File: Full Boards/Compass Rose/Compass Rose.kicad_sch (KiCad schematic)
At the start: 249 parts, among them J1 Program Header, J3 Optional Bond, Q1 BSS314PE, Q2 DMN6075S, Q3 BSS314PE, Q4 DMN6075S, Q5 BSS314PE, Q6 DMN6075S, SW1 Boot, SW2 Reset, SW3 219-2MSTR

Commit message: Updated the 100uF caps to polymer.
Signed-off-by: digimer <digital.mermaid@gmail.com>
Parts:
- C19, C20, C21: footprint Capacitor_THT:CP_Radial_D8.0mm_P5.00mm -> Capacitor_THT:CP_Radial_D8.0mm_P3.50mm; Part Nichicon UPW1H101MPD1FA -> Kemet A7C0KS107M1HAAS031

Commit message: Swapped the 10uF cap to a ceramic.
Signed-off-by: digimer <digital.mermaid@gmail.com>
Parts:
- C5: footprint mr-stuff:Nichicon UBT -> mr-stuff:Kyocera AVX 1206; Part Nichicon UBT1H100MPD8 -> Kyocera 12105C106K4Z2A
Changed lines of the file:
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@@
 			)
 		)
-		(property "Footprint" "mr-stuff:Nichicon UBT"
+		(property "Footprint" "mr-stuff:Kyocera AVX 1206"
 			(at 200.3552 35.56 0)
 			(hide yes)
@@
 			)
 		)
-		(property "Datasheet" "https://www.nichicon.co.jp/english/series_items/catalog_pdf/e-ubt.pdf"
+		(property "Datasheet" "https://datasheets.kyocera-avx.com/FlexitermMLCC.pdf"
 			(at 199.39 31.75 0)
 			(hide yes)
@@
 			)
 		)
-		(property "Description" "10 µF 50 V Aluminum Electrolytic Capacitors Radial, Can 2000 Hrs @ 125°C"
+		(property "Description" "10 µF ±10% 50V Ceramic Capacitor X7R 1210 (3225 Metric)"
 			(at 199.39 31.75 0)
 			(hide yes)
@@
 			)
 		)
-		(property "Part" "Nichicon UBT1H100MPD8"
+		(property "Part" "Kyocera 12105C106K4Z2A"
 			(at 199.39 31.75 0)
 			(hide yes)

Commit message: Restarted layout of PCB after LED ring corruption.
Signed-off-by: digimer <digital.mermaid@gmail.com>
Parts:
- SW3: value 219-2MSTR -> CTS_219-2MSTR; footprint (none) -> mr-stuff:CTS 219-2MSTR
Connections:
- net +5V: now also R17.2; no longer R17.1
- net CONFIG_1: now also SW3.1A; no longer SW3.1
- net CONFIG_2: now also SW3.2A; no longer SW3.2
- net GND: now also C27.1; no longer C27.2
- net at LCD2.6 (SCL), LS1.6 (SCL2): now also R17.1; no longer R17.2
- net at C28.2, LS1.7 (VREF2), LS1.8 (EN)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: now also C27.2; no longer C27.1
- net at R2.2: now also SW3.2B; no longer SW3.3
- net at R1.2: now also SW3.1B; no longer SW3.4
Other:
- moved on the sheet: R17, R19, R20, TP5
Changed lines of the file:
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@@
 	(rectangle
 		(start 15.24 127.508)
-		(end 78.994 198.12)
+		(end 114.935 198.12)
 		(stroke
 			(width 0)
@@
 		)
 	)
-	(text "NOTE: \nIS31FL373Ω is powered from the +5V rail to allow for higher\nvoltage LEDs. The I2C bus operates natively at 3.3V. This\nlogic mismatch is validated. The minimum High-Level Input\nVoltage V{IH} of 1.4V. The 3.3V logic exceeds this threshold.\nA level shifter is intentionally omitted."
+	(text "NOTE: \nIS31FL373Ω is powered from the +5V rail to allow for higher voltage LEDs. The I2C bus operates\nnatively at 3.3V. This logic mismatch is validated. The minimum High-Level Input Voltage V{IH}\nof 1.4V. The 3.3V logic exceeds this threshold. A level shifter is intentionally omitted."
 		(exclude_from_sim no)
-		(at 16.764 186.182 0)
+		(at 16.256 189.738 0)
 		(effects
 			(font
@@
 	)
 	(junction
-		(at 240.03 224.79)
+		(at 96.52 146.05)
 		(diameter 0)
 		(color 0 0 0 0)
@@
 	)
 	(junction
-		(at 248.92 227.33)
+		(at 105.41 148.59)
 		(diameter 0)
 		(color 0 0 0 0)
@@
 	(wire
 		(pts
-			(xy 248.92 227.33) (xy 254 227.33)
+			(xy 105.41 148.59) (xy 110.49 148.59)
 		)
 		(stroke
@@
 	(wire
 		(pts
-			(xy 254 222.25) (xy 254 227.33)
+			(xy 110.49 143.51) (xy 110.49 148.59)
 		)
 		(stroke
@@
 	(wire
 		(pts
-			(xy 240.03 213.36) (xy 240.03 214.63)
+			(xy 96.52 134.62) (xy 96.52 135.89)
 		)
 		(stroke
@@
 	(wire
 		(pts
-			(xy 237.49 224.79) (xy 240.03 224.79)
+			(xy 93.98 146.05) (xy 96.52 146.05)
 		)
 		(stroke
@@
 	(wire
 		(pts
-			(xy 246.38 218.44) (xy 246.38 224.79)
+			(xy 102.87 139.7) (xy 102.87 146.05)
 		)
 		(stroke
@@
 	(wire
 		(pts
-			(xy 237.49 227.33) (xy 248.92 227.33)
+			(xy 93.98 148.59) (xy 105.41 148.59)
 		)
 		(stroke
@@
 	(wire
 		(pts
-			(xy 254 214.63) (xy 254 213.36)
+			(xy 110.49 135.89) (xy 110.49 134.62)
 		)
 		(stroke
@@
 	(wire
 		(pts
-			(xy 246.38 224.79) (xy 240.03 224.79)
+			(xy 102.87 146.05) (xy 96.52 146.05)
 		)
 		(stroke
@@
 	(wire
 		(pts
-			(xy 240.03 222.25) (xy 240.03 224.79)
+			(xy 96.52 143.51) (xy 96.52 146.05)
 		)
 		(stroke
@@
 	(wire
 		(pts
-			(xy 248.92 227.33) (xy 248.92 218.44)
+			(xy 105.41 148.59) (xy 105.41 139.7)
 		)
 		(stroke
@@
 	)
 	(label "IS31_I2C_SDA"
-		(at 237.49 224.79 180)
+		(at 93.98 146.05 180)
 		(effects
 			(font
@@
 	)
 	(label "IS31_I2C_SCL"
-		(at 237.49 227.33 180)
+		(at 93.98 148.59 180)
 		(effects
 			(font
@@
 	(symbol
 		(lib_id "Device:R")
-		(at 205.74 161.29 90)
+		(at 205.74 161.29 270)
 		(unit 1)
 		(body_style 1)
@@
 		(dnp no)
 		(property "Reference" "R17"
-			(at 207.518 161.29 90)
+			(at 203.962 161.29 90)
 			(show_name no)
 			(do_not_autoplace no)
@@
 		)
 		(property "Value" "4.7k"
-			(at 208.026 159.004 90)
+			(at 203.708 159.258 90)
 			(show_name no)
 			(do_not_autoplace no)
@@
 		)
 		(property "Footprint" "mr-stuff:Stackpole RMCA0805"
-			(at 205.74 163.068 90)
+			(at 205.74 159.512 90)
 			(hide yes)
 			(show_name no)
@@
 	(symbol
 		(lib_id "power:+3.3V")
-		(at 240.03 213.36 0)
+		(at 96.52 134.62 0)
 		(unit 1)
 		(body_style 1)
@@
 		(dnp no)
 		(property "Reference" "#PWR015"
-			(at 240.03 217.17 0)
+			(at 96.52 138.43 0)
 			(hide yes)
 			(show_name no)
@@
 		)
 		(property "Value" "+3.3V"
-			(at 240.03 209.55 0)
+			(at 96.52 130.81 0)
 			(show_name no)
 			(do_not_autoplace no)
@@
 		)
 		(property "Footprint" ""
-			(at 240.03 213.36 0)
+			(at 96.52 134.62 0)
 			(hide yes)
 			(show_name no)
@@
 		)
 		(property "Datasheet" ""
-			(at 240.03 213.36 0)
+			(at 96.52 134.62 0)
 			(hide yes)
 			(show_name no)
@@
 		)
 		(property "Description" "Power symbol creates a global label with name \"+3.3V\""
-			(at 240.03 213.36 0)
+			(at 96.52 134.62 0)
 			(hide yes)
 			(show_name no)
@@
 	(symbol
 		(lib_id "Device:R")
-		(at 240.03 218.44 180)
+		(at 96.52 139.7 180)
 		(unit 1)
 		(body_style 1)
@@
 		(dnp no)
 		(property "Reference" "R19"
-			(at 240.03 218.44 90)
+			(at 96.52 139.7 90)
 			(show_name no)
 			(do_not_autoplace no)
@@
 		)
 		(property "Value" "3.3k"
-			(at 237.744 218.186 90)
+			(at 94.234 139.446 90)
 			(show_name no)
 			(do_not_autoplace no)
@@
 		)
 		(property "Footprint" "mr-stuff:Stackpole RNCF0805"
-			(at 241.808 218.44 90)
+			(at 98.298 139.7 90)
 			(hide yes)
 			(show_name no)
@@
 		)
 		(property "Datasheet" "https://www.seielect.com/catalog/SEI-RNCF.pdf"
-			(at 240.03 218.44 0)
+			(at 96.52 139.7 0)
 			(hide yes)
 			(show_name no)
@@
 		)
 		(property "Description" "3.3 kOhms ±0.5% 0.25W, 1/4W Chip Resistor 0805 (2012 Metric) Automotive AEC-Q200 Thin Film"
-			(at 240.03 218.44 0)
+			(at 96.52 139.7 0)
 			(hide yes)
 			(show_name no)
@@
 		)
 		(property "Part" "Stackpole RNCF0805DTE3K30"
-			(at 240.03 218.44 90)
+			(at 96.52 139.7 90)
 			(hide yes)
 			(show_name no)
@@
 			)
 		)
-		(property "Value" "219-2MSTR"
+		(property "Value" "CTS_219-2MSTR"
 			(at 218.44 114.3 0)
 			(show_name no)
@@
 			)
 		)
-		(property "Footprint" ""
-			(at 218.44 109.22 0)
+		(property "Footprint" "mr-stuff:CTS 219-2MSTR"
+			(at 218.44 123.444 0)
 			(hide yes)
 			(show_name no)
@@
 			)
 		)
-		(property "Datasheet" ""
-			(at 218.44 109.22 0)
+		(property "Datasheet" "https://www.ctscorp.com/Files/DataSheets/Switches/DIP-Switches/CTS-Switches-DIP-219-Series-Datasheet.pdf"
+			(at 218.44 116.84 0)
 			(hide yes)
 			(show_name no)
@@
 			)
 		)
-		(property "Description" "2x DIP Switch, Single Pole Single Throw (SPST) switch, small symbol"
-			(at 218.44 109.22 0)
+		(property "Description" "Dip Switch SPST 2 Position Surface Mount Slide (Standard) Actuator 100mA 20VDC"
+			(at 218.186 119.126 0)
 			(hide yes)
 			(show_name no)
@@
 			)
 		)
-		(pin "2"
+		(pin "1B"
 		)
-		(pin "3"
+		(pin "2B"
 		)
-		(pin "4"
+		(pin "2A"
 		)
-		(pin "1"
+		(pin "1A"
 		)
 		(instances
@@
 		(lib_name "Conn_01x02_Pin_1")
 		(lib_id "Connector:Conn_01x02_Pin")
-		(at 246.38 213.36 90)
+		(at 102.87 134.62 90)
 		(mirror x)
 		(unit 1)
@@
 		(dnp no)
 		(property "Reference" "TP5"
-			(at 249.936 210.058 90)
+			(at 106.426 131.318 90)
 			(show_name no)
 			(do_not_autoplace no)
@@
 		)
 		(property "Value" "IS31 I2C"
-			(at 251.714 212.09 90)
+			(at 108.204 133.35 90)
 			(show_name no)
 			(do_not_autoplace no)
@@
 		)
 		(property "Footprint" "Connector_PinHeader_2.54mm:PinHeader_1x02_P2.54mm_Vertical"
-			(at 246.38 213.36 0)
+			(at 102.87 134.62 0)
 			(hide yes)
 			(show_name no)
@@
 		)
 		(property "Datasheet" ""
-			(at 246.38 213.36 0)
+			(at 102.87 134.62 0)
 			(hide yes)
 			(show_name no)
@@
 		)
 		(property "Description" "Generic connector, single row, 01x02, script generated"
-			(at 246.38 213.36 0)
+			(at 102.87 134.62 0)
 			(hide yes)
 			(show_name no)
@@
 	(symbol
 		(lib_id "power:+3.3V")
-		(at 254 213.36 0)
+		(at 110.49 134.62 0)
 		(unit 1)
 		(body_style 1)
@@
 		(dnp no)
 		(property "Reference" "#PWR018"
-			(at 254 217.17 0)
+			(at 110.49 138.43 0)
 			(hide yes)
 			(show_name no)
@@
 		)
 		(property "Value" "+3.3V"
-			(at 254 209.55 0)
+			(at 110.49 130.81 0)
 			(show_name no)
 			(do_not_autoplace no)
@@
 		)
 		(property "Footprint" ""
-			(at 254 213.36 0)
+			(at 110.49 134.62 0)
 			(hide yes)
 			(show_name no)
@@
 		)
 		(property "Datasheet" ""
-			(at 254 213.36 0)
+			(at 110.49 134.62 0)
 			(hide yes)
 			(show_name no)
@@
 		)
 		(property "Description" "Power symbol creates a global label with name \"+3.3V\""
-			(at 254 213.36 0)
+			(at 110.49 134.62 0)
 			(hide yes)
 			(show_name no)
@@
 	(symbol
 		(lib_id "Device:R")
-		(at 254 218.44 180)
+		(at 110.49 139.7 180)
 		(unit 1)
 		(body_style 1)
@@
 		(dnp no)
 		(property "Reference" "R20"
-			(at 254 218.44 90)
+			(at 110.49 139.7 90)
 			(show_name no)
 			(do_not_autoplace no)
@@
 		)
 		(property "Value" "3.3k"
-			(at 251.714 218.186 90)
+			(at 108.204 139.446 90)
 			(show_name no)
 			(do_not_autoplace no)
@@
 		)
 		(property "Footprint" "mr-stuff:Stackpole RNCF0805"
-			(at 255.778 218.44 90)
+			(at 112.268 139.7 90)
 			(hide yes)
 			(show_name no)
@@
 		)
 		(property "Datasheet" "https://www.seielect.com/catalog/SEI-RNCF.pdf"
-			(at 254 218.44 0)
+			(at 110.49 139.7 0)
 			(hide yes)
 			(show_name no)
@@
 		)
 		(property "Description" "3.3 kOhms ±0.5% 0.25W, 1/4W Chip Resistor 0805 (2012 Metric) Automotive AEC-Q200 Thin Film"
-			(at 254 218.44 0)
+			(at 110.49 139.7 0)
 			(hide yes)
 			(show_name no)
@@
 		)
 		(property "Part" "Stackpole RNCF0805DTE3K30"
-			(at 254 218.44 90)
+			(at 110.49 139.7 90)
 			(hide yes)
 			(show_name no)
@@
 		(lib_id "Device:C")
 		(at 201.93 179.07 0)
-		(mirror y)
+		(mirror x)
 		(unit 1)
 		(body_style 1)
@@
 		(dnp no)
 		(property "Reference" "C27"
-			(at 201.422 176.784 0)
+			(at 197.866 176.784 0)
 			(show_name no)
 			(do_not_autoplace no)
@@
 		)
 		(property "Value" "0.01uF"
-			(at 201.422 181.356 0)
+			(at 195.072 181.61 0)
 			(show_name no)
 			(do_not_autoplace no)
@@
 		)
 		(property "Footprint" "mr-stuff:Kemet C0805X"
-			(at 200.9648 182.88 0)
+			(at 202.8952 175.26 0)
 			(hide yes)
 			(show_name no)

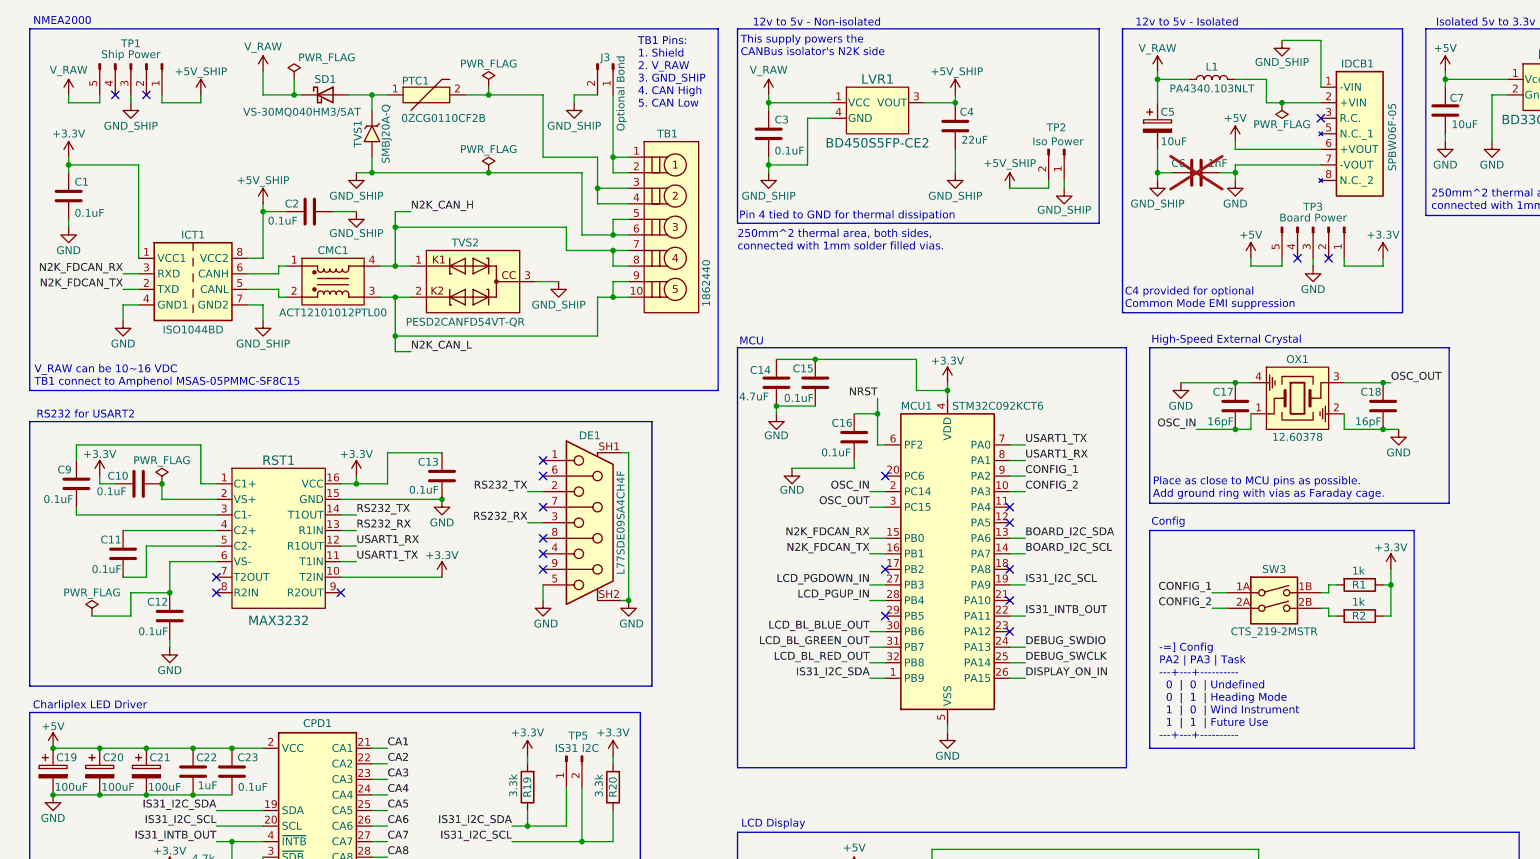
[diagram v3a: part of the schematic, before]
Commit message: Added the rest of the power blocks.
Signed-off-by: digimer <digital.mermaid@gmail.com>
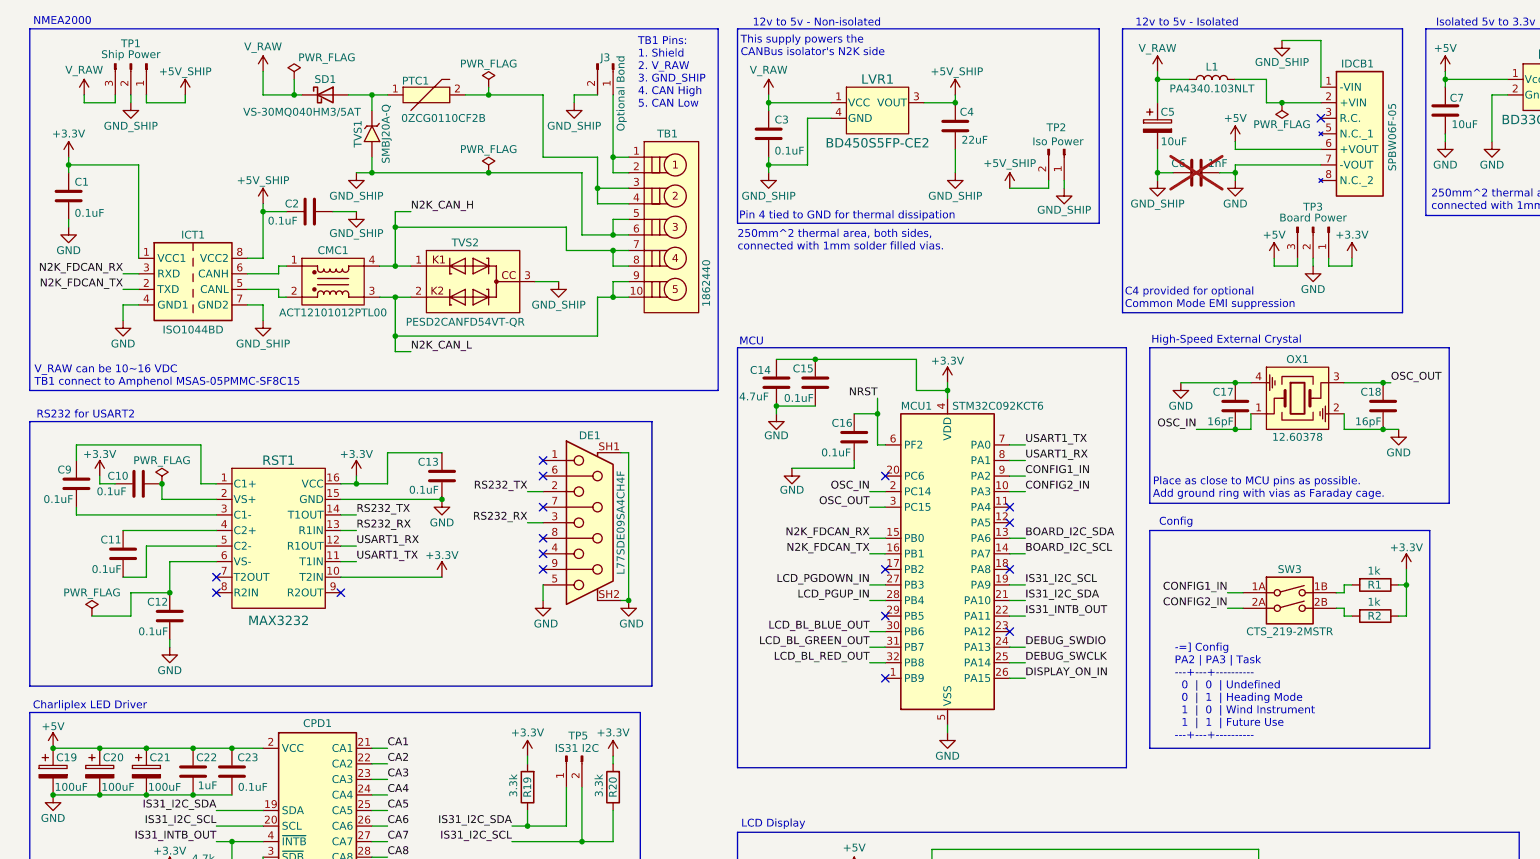
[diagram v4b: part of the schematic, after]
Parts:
- TP1, TP3: footprint Connector_PinHeader_2.54mm:PinHeader_1x05_P2.54mm_Vertical -> Connector_PinHeader_2.54mm:PinHeader_1x03_P2.54mm_Vertical; symbol Connector:Conn_01x05_Pin -> Connector:Conn_01x03_Pin
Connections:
- net +5V: now also TP3.3 (Pin_3); no longer TP3.5 (Pin_5)
- net GND: now also TP3.2 (Pin_2); no longer TP3.3 (Pin_3)
- net GND_SHIP: now also TP1.2 (Pin_2); no longer TP1.3 (Pin_3)
- net IS31_I2C_SDA: now also MCU1.21 (PA10); no longer MCU1.1 (PB9)
- net V_RAW: now also TP1.3 (Pin_3); no longer TP1.5 (Pin_5)
- net CONFIG_1 renamed CONFIG1_IN
- net CONFIG_2 renamed CONFIG2_IN
- no-connect marks 28 -> 24
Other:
- moved on the sheet: R1, R2, SW3

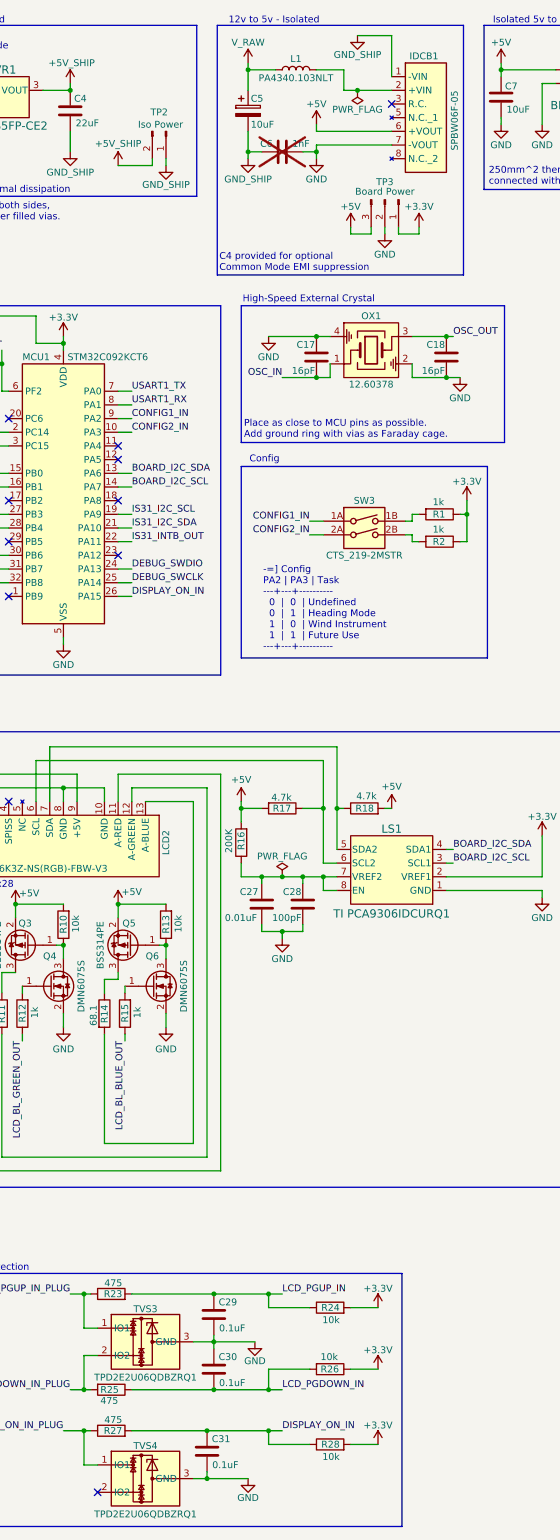
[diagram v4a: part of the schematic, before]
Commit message: Mostly laid out, but KiCAD crashed. Committing work before recovery.
Signed-off-by: digimer <digital.mermaid@gmail.com>
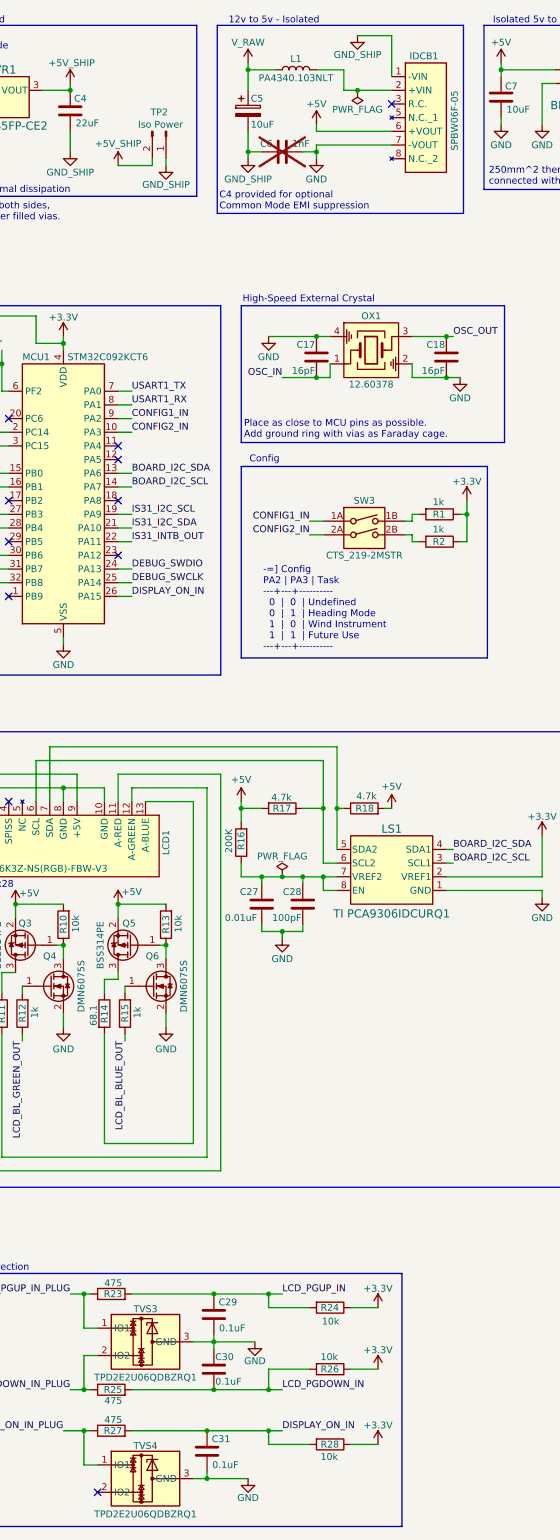
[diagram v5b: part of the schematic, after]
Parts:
- removed TP3: Board Power, Connector_PinHeader_2.54mm:PinHeader_1x03_P2.54mm_Vertical, symbol Connector:Conn_01x03_Pin
- renumbered LCD2 to LCD1
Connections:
- net +3.3V: now also R24.1, R28.1; no longer R24.2, R28.2
- net DISPLAY_ON_IN: now also R28.2; no longer R28.1
- net GND: now also C30.1; no longer C30.2
- net LCD_PGDOWN_IN: now also C30.2, R25.2; no longer C30.1, R25.1
- net LCD_PGDOWN_IN_PLUG: now also R25.1; no longer R25.2
- net LCD_PGUP_IN: now also R24.2; no longer R24.1
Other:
- moved on the sheet: C30, R24, R25, R28
